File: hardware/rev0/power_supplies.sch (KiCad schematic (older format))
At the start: 40 parts, among them IC1 ECP5-BGA256, U2 MIC5504-1.8YM5, U3 MIC5219-3.3YM5, U4 TCR2EF11, U5 MIC5504-2.5YM5

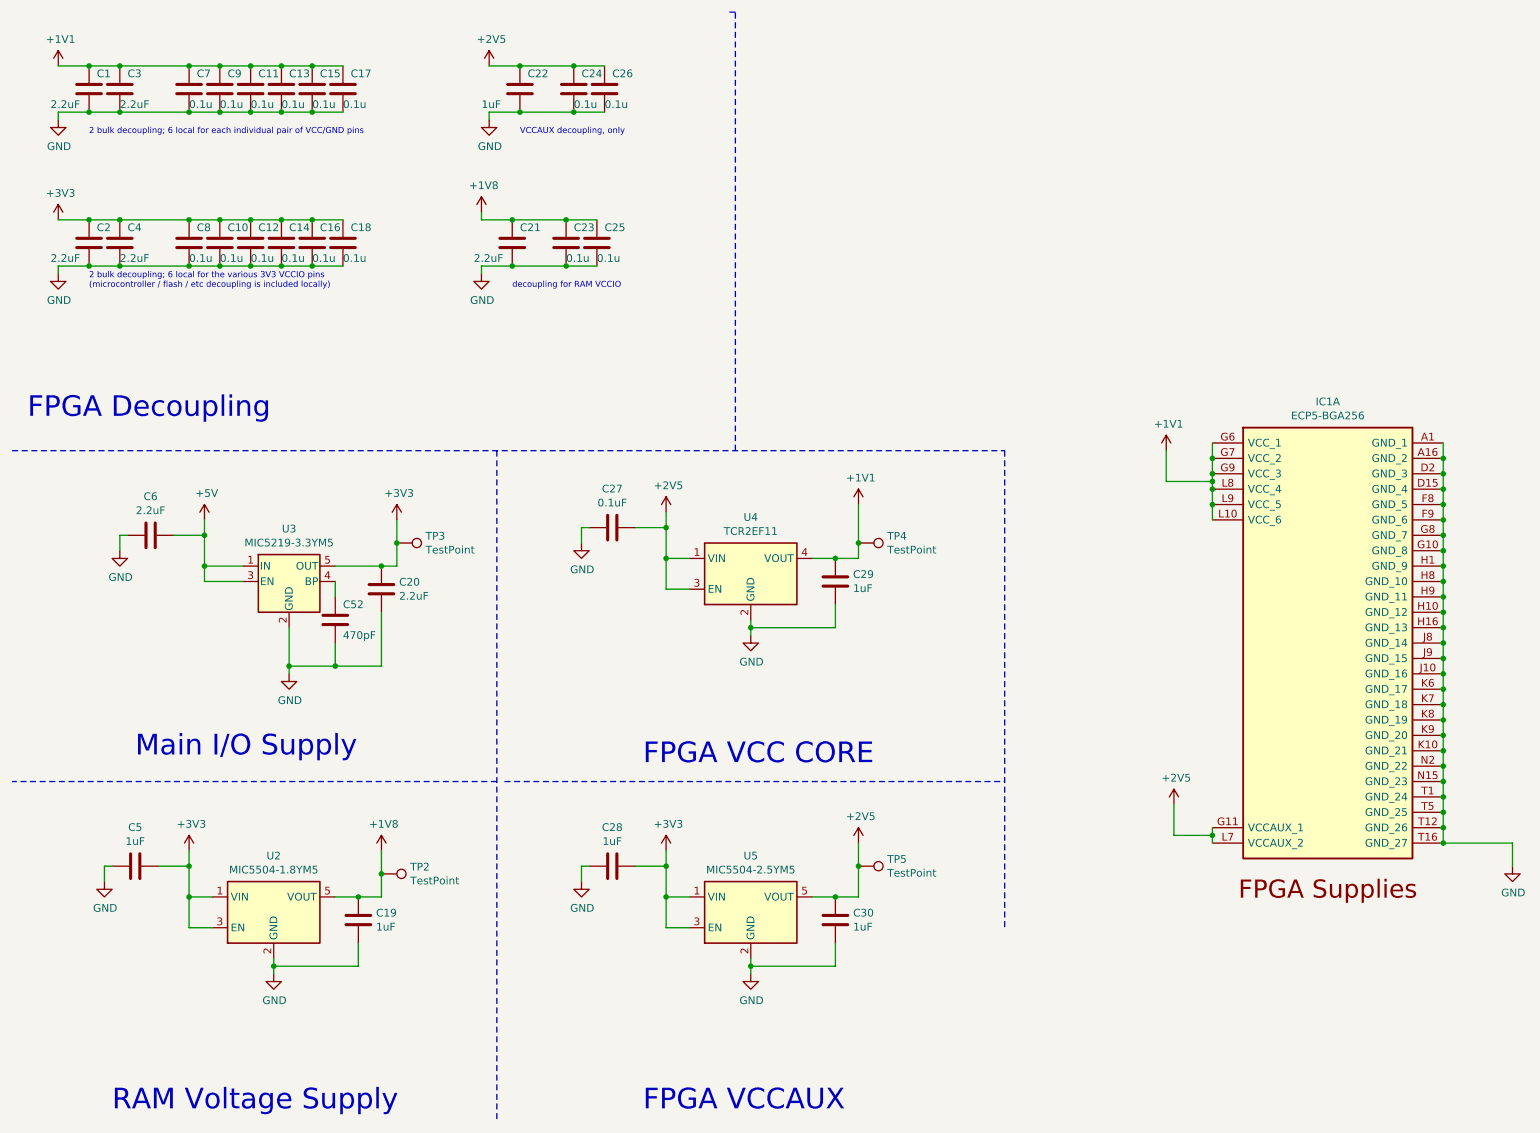
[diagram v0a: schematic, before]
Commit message: Switch to 3V3 for RAM, remove 1V8 rail
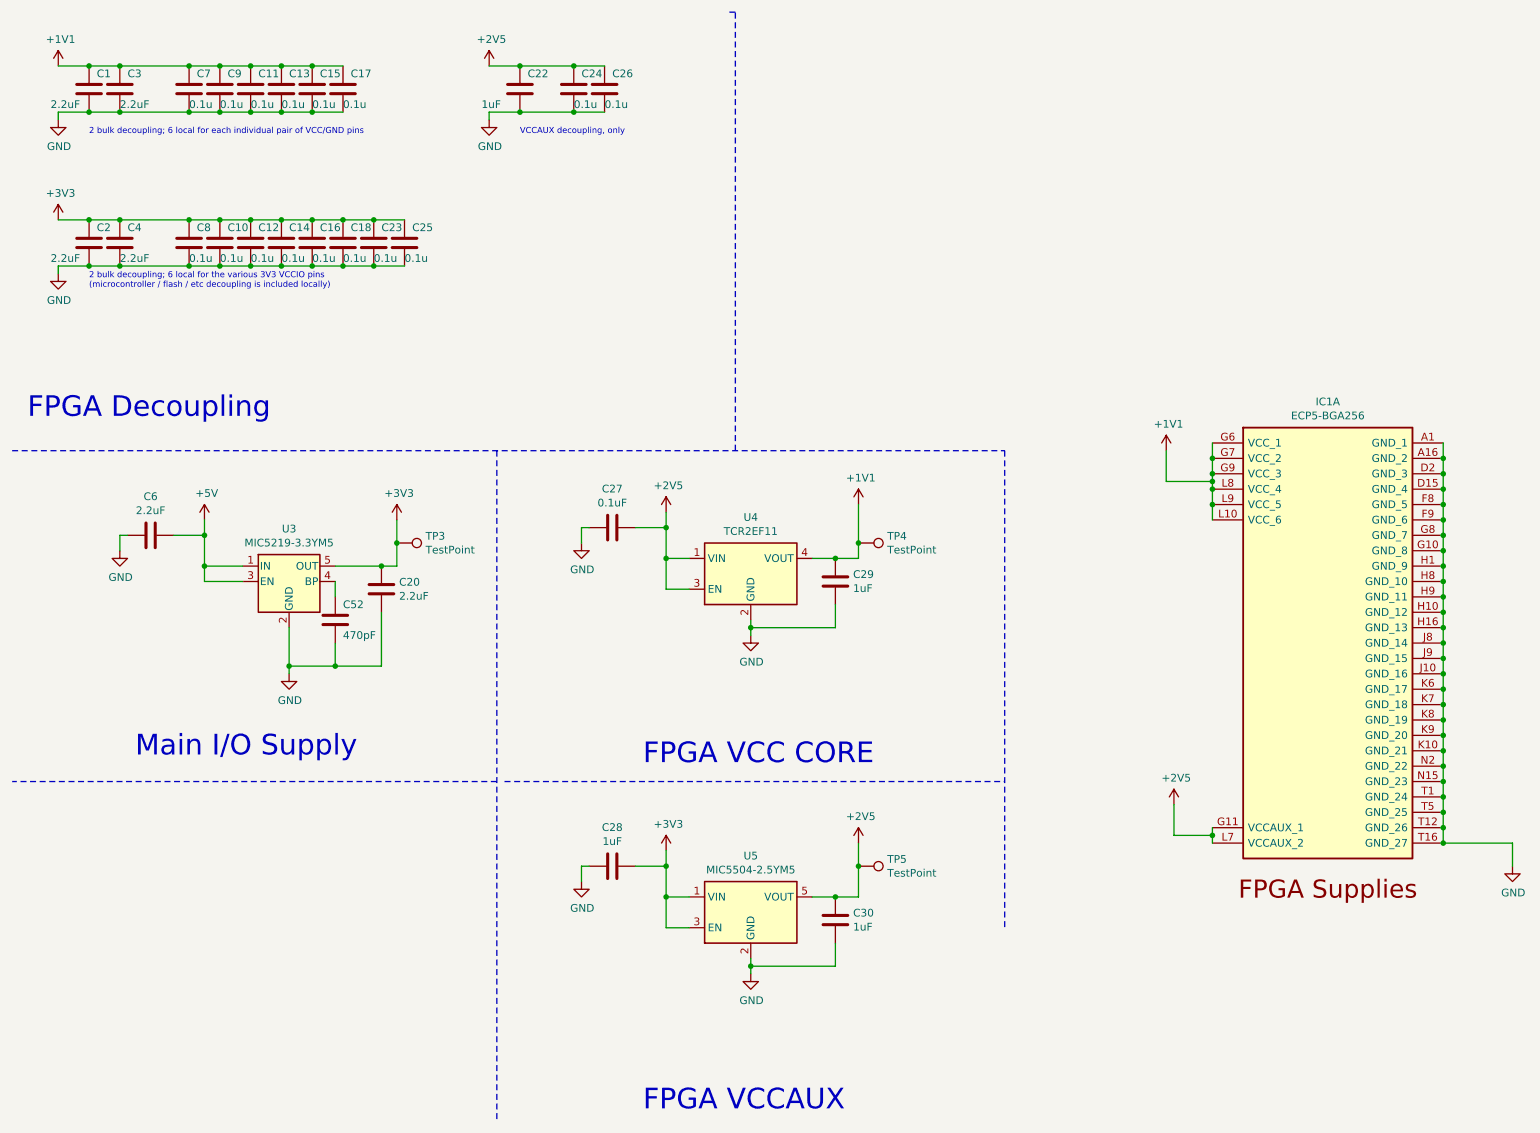
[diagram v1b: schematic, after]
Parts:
- removed C19, C5: 1uF, Capacitor_SMD:C_0603_1608Metric, symbol Device:C
- removed C21: 2.2uF, Capacitor_SMD:C_0603_1608Metric, symbol Device:C
- removed TP2: TestPoint, TestPoint:TestPoint_Pad_D1.0mm, symbol Connector:TestPoint
- removed U2: MIC5504-1.8YM5, Package_TO_SOT_SMD:SOT-23-5, symbol Regulator_Linear:MIC5504-1.8YM5
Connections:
- net +1V8 is gone; now on net +3V3: C23.1, C25.1
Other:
- note removed: "RAM Voltage Supply"
- note removed: "decoupling for RAM VCCIO"
- moved on the sheet: C23, C25
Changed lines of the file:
@@
 	1    0    0    -1
 $EndComp
-$Comp
-L Regulator_Linear:MIC5504-1.8YM5 U2
-U 1 1 5DAC1E40
-P 2250 6350
-F 0 "U2" H 2250 6717 50  0000 C CNN
-F 1 "MIC5504-1.8YM5" H 2250 6626 50  0000 C CNN
-F 2 "Package_TO_SOT_SMD:SOT-23-5" H 2250 5950 50  0001 C CNN
-F 3 "http://ww1.microchip.com/downloads/en/DeviceDoc/MIC550X.pdf" H 2000 6600 50  0001 C CNN
-	1    2250 6350
-	1    0    0    -1
-$EndComp
-Wire Wire Line
-	1850 6250 1700 6250
-$Comp
-L power:+3V3 #PWR018
-U 1 1 5DAC56AB
-P 1700 5950
-F 0 "#PWR018" H 1700 5800 50  0001 C CNN
-F 1 "+3V3" H 1715 6123 50  0000 C CNN
-F 2 "" H 1700 5950 50  0001 C CNN
-F 3 "" H 1700 5950 50  0001 C CNN
-	1    1700 5950
-	1    0    0    -1
-$EndComp
-Wire Wire Line
-	2250 6650 2250 6700
-$Comp
-L power:GND #PWR020
-U 1 1 5DAC8A3A
-P 2250 6750
-F 0 "#PWR020" H 2250 6500 50  0001 C CNN
-F 1 "GND" H 2255 6577 50  0000 C CNN
-F 2 "" H 2250 6750 50  0001 C CNN
-F 3 "" H 2250 6750 50  0001 C CNN
-	1    2250 6750
-	1    0    0    -1
-$EndComp
-Wire Wire Line
-	1700 5950 1700 6050
-$Comp
-L Device:C C5
-U 1 1 5DACA9F3
-P 1350 6050
-F 0 "C5" V 1098 6050 50  0000 C CNN
-F 1 "1uF" V 1189 6050 50  0000 C CNN
-F 2 "Capacitor_SMD:C_0603_1608Metric" H 1388 5900 50  0001 C CNN
-F 3 "~" H 1350 6050 50  0001 C CNN
-	1    1350 6050
-	0    1    1    0
-$EndComp
-Wire Wire Line
-	1150 6050 1200 6050
-Wire Wire Line
-	1150 6150 1150 6050
-$Comp
-L power:GND #PWR016
-U 1 1 5DACD5E8
-P 1150 6150
-F 0 "#PWR016" H 1150 5900 50  0001 C CNN
-F 1 "GND" H 1155 5977 50  0000 C CNN
-F 2 "" H 1150 6150 50  0001 C CNN
-F 3 "" H 1150 6150 50  0001 C CNN
-	1    1150 6150
-	1    0    0    -1
-$EndComp
-Connection ~ 1700 6050
-Wire Wire Line
-	1700 6050 1700 6250
-Wire Wire Line
-	2650 6250 2800 6250
-$Comp
-L power:+1V8 #PWR022
-U 1 1 5DAD001F
-P 2950 5950
-F 0 "#PWR022" H 2950 5800 50  0001 C CNN
-F 1 "+1V8" H 2965 6123 50  0000 C CNN
-F 2 "" H 2950 5950 50  0001 C CNN
-F 3 "" H 2950 5950 50  0001 C CNN
-	1    2950 5950
-	1    0    0    -1
-$EndComp
-Wire Wire Line
-	2950 5950 2950 6100
-$Comp
-L Device:C C19
-U 1 1 5DAD4777
-P 2800 6400
-F 0 "C19" H 2915 6446 50  0000 L CNN
-F 1 "1uF" H 2915 6355 50  0000 L CNN
-F 2 "Capacitor_SMD:C_0603_1608Metric" H 2838 6250 50  0001 C CNN
-F 3 "~" H 2800 6400 50  0001 C CNN
-	1    2800 6400
-	1    0    0    -1
-$EndComp
-Connection ~ 2800 6250
-Wire Wire Line
-	2800 6250 2950 6250
-Wire Wire Line
-	2800 6550 2800 6700
-Wire Wire Line
-	2800 6700 2250 6700
-Connection ~ 2250 6700
-Wire Wire Line
-	2250 6700 2250 6750
-Text Notes 1200 7650 0    134  ~ 0
-RAM Voltage Supply
 Wire Wire Line
 	4950 6250 4800 6250
@@
 $EndComp
 $Comp
-L Device:C C18
-U 1 1 5DBA82B3
-P 2700 2000
-F 0 "C18" H 2750 2100 50  0000 L CNN
-F 1 "0.1u" H 2700 1900 50  0000 L CNN
-F 2 "Capacitor_SMD:C_0402_1005Metric" H 2738 1850 50  0001 C CNN
-F 3 "~" H 2700 2000 50  0001 C CNN
-	1    2700 2000
-	1    0    0    -1
-$EndComp
-$Comp
 L Device:C C16
 U 1 1 5DBA82A9
@@
 Wire Wire Line
 	3850 850  4200 850
-Text Notes 3800 2300 0    39   ~ 0
-decoupling for RAM VCCIO
-$Comp
-L power:GND #PWR025
-U 1 1 5DC15F71
-P 3600 2200
-F 0 "#PWR025" H 3600 1950 50  0001 C CNN
-F 1 "GND" H 3605 2027 50  0000 C CNN
-F 2 "" H 3600 2200 50  0001 C CNN
-F 3 "" H 3600 2200 50  0001 C CNN
-	1    3600 2200
-	1    0    0    -1
-$EndComp
-Connection ~ 4150 2150
-Wire Wire Line
-	3800 2150 3600 2150
-Connection ~ 3800 2150
-Wire Wire Line
-	3600 2150 3600 2200
-Connection ~ 4150 1850
-Connection ~ 3800 1850
-Wire Wire Line
-	3600 1850 3800 1850
-$Comp
-L Device:C C21
-U 1 1 5DC15F82
-P 3800 2000
-F 0 "C21" H 3850 2100 50  0000 L CNN
-F 1 "2.2uF" H 3550 1900 50  0000 L CNN
-F 2 "Capacitor_SMD:C_0603_1608Metric" H 3838 1850 50  0001 C CNN
-F 3 "~" H 3800 2000 50  0001 C CNN
-	1    3800 2000
-	1    0    0    -1
-$EndComp
-$Comp
-L Device:C C23
-U 1 1 5DC15F8C
-P 4150 2000
-F 0 "C23" H 4200 2100 50  0000 L CNN
-F 1 "0.1u" H 4150 1900 50  0000 L CNN
-F 2 "Capacitor_SMD:C_0402_1005Metric" H 4188 1850 50  0001 C CNN
-F 3 "~" H 4150 2000 50  0001 C CNN
-	1    4150 2000
-	1    0    0    -1
-$EndComp
-Wire Wire Line
-	4350 2150 4150 2150
-Wire Wire Line
-	4150 1850 4350 1850
-$Comp
-L Device:C C25
-U 1 1 5DC15FA2
-P 4350 2000
-F 0 "C25" H 4400 2100 50  0000 L CNN
-F 1 "0.1u" H 4350 1900 50  0000 L CNN
-F 2 "Capacitor_SMD:C_0402_1005Metric" H 4388 1850 50  0001 C CNN
-F 3 "~" H 4350 2000 50  0001 C CNN
-	1    4350 2000
-	1    0    0    -1
-$EndComp
-Wire Wire Line
-	3800 2150 4150 2150
-Wire Wire Line
-	3800 1850 4150 1850
-$Comp
-L power:+1V8 #PWR024
-U 1 1 5DC20A72
-P 3600 1800
-F 0 "#PWR024" H 3600 1650 50  0001 C CNN
-F 1 "+1V8" H 3615 1973 50  0000 C CNN
-F 2 "" H 3600 1800 50  0001 C CNN
-F 3 "" H 3600 1800 50  0001 C CNN
-	1    3600 1800
-	1    0    0    -1
-$EndComp
-Wire Wire Line
-	3600 1800 3600 1850
 Wire Notes Line
 	5250 3350 5250 500
@@
 Wire Wire Line
 	4800 4250 4950 4250
-Wire Wire Line
-	1500 6050 1700 6050
-Wire Wire Line
-	1850 6450 1700 6450
-Wire Wire Line
-	1700 6450 1700 6250
-Connection ~ 1700 6250
 Wire Wire Line
 	4800 6250 4800 6450
@@
 	6050 6050 6050 6250
 $Comp
-L Connector:TestPoint TP2
-U 1 1 5E2192C9
-P 2950 6100
-F 0 "TP2" V 2905 6287 50  0000 L CNN
-F 1 "TestPoint" V 2995 6287 50  0000 L CNN
-F 2 "TestPoint:TestPoint_Pad_D1.0mm" H 3150 6100 50  0001 C CNN
-F 3 "~" H 3150 6100 50  0001 C CNN
-	1    2950 6100
-	0    1    1    0
-$EndComp
-Connection ~ 2950 6100
-Wire Wire Line
-	2950 6100 2950 6250
+L Device:C C25
+U 1 1 5DC15FA2
+P 3100 2000
+F 0 "C25" H 3150 2100 50  0000 L CNN
+F 1 "0.1u" H 3100 1900 50  0000 L CNN
+F 2 "Capacitor_SMD:C_0402_1005Metric" H 3138 1850 50  0001 C CNN
+F 3 "~" H 3100 2000 50  0001 C CNN
+	1    3100 2000
+	1    0    0    -1
+$EndComp
+$Comp
+L Device:C C23
+U 1 1 5DC15F8C
+P 2900 2000
+F 0 "C23" H 2950 2100 50  0000 L CNN
+F 1 "0.1u" H 2900 1900 50  0000 L CNN
+F 2 "Capacitor_SMD:C_0402_1005Metric" H 2938 1850 50  0001 C CNN
+F 3 "~" H 2900 2000 50  0001 C CNN
+	1    2900 2000
+	1    0    0    -1
+$EndComp
+Wire Wire Line
+	2900 1850 3100 1850
+Wire Wire Line
+	3100 2150 2900 2150
+$Comp
+L Device:C C18
+U 1 1 5DBA82B3
+P 2700 2000
+F 0 "C18" H 2750 2100 50  0000 L CNN
+F 1 "0.1u" H 2700 1900 50  0000 L CNN
+F 2 "Capacitor_SMD:C_0402_1005Metric" H 2738 1850 50  0001 C CNN
+F 3 "~" H 2700 2000 50  0001 C CNN
+	1    2700 2000
+	1    0    0    -1
+$EndComp
+Wire Wire Line
+	2700 1850 2900 1850
+Connection ~ 2700 1850
+Connection ~ 2900 1850
+Wire Wire Line
+	2700 2150 2900 2150
+Connection ~ 2700 2150
+Connection ~ 2900 2150
 $EndSCHEMATC

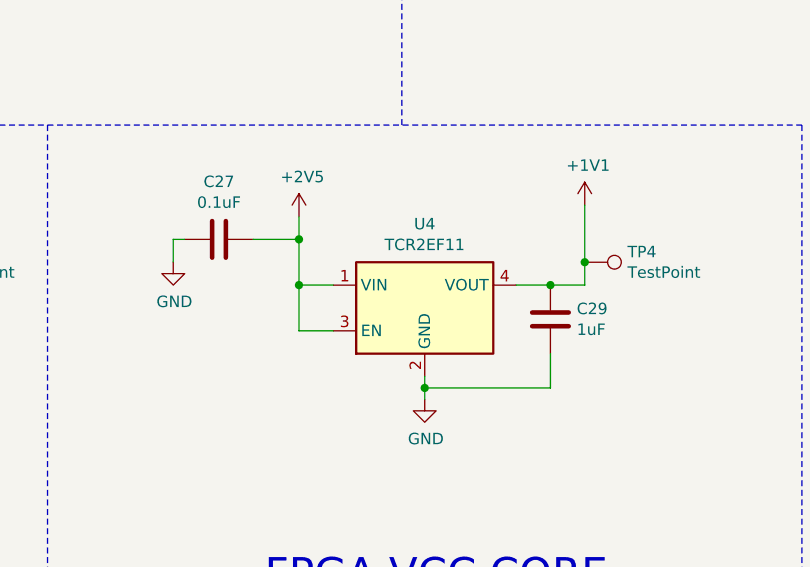
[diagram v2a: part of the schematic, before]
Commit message: Fix TCR2EE footprint
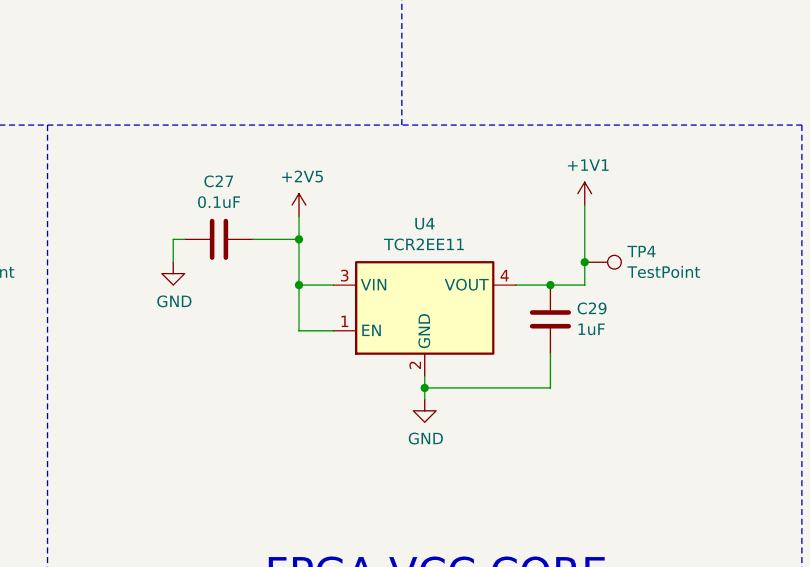
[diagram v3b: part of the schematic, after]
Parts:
- removed U4: TCR2EF11, Package_TO_SOT_SMD:SOT-553, symbol support_hardware:TCR2EF11
- added U4: TCR2EE11, Package_TO_SOT_SMD:SOT-553, symbol support_hardware:TCR2EE11
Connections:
- net +1V1: now also U4.4 (VOUT)
- net +2V5: now also U4.1 (EN), U4.3 (VIN)
- net GND: now also U4.2 (GND)
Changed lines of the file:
@@
 	550  3350 7000 3350
-$Comp
-L support_hardware:TCR2EF11 U4
-U 1 1 5DB6F5E4
-P 5350 4150
-F 0 "U4" H 5350 4517 50  0000 C CNN
-F 1 "TCR2EF11" H 5350 4426 50  0000 C CNN
-F 2 "Package_TO_SOT_SMD:SOT-553" H 5350 3750 50  0001 C CNN
-F 3 "https://toshiba.semicon-storage.com/info/docget.jsp?did=13794&prodName=TCR2EF45" H 5100 4400 50  0001 C CNN
-	1    5350 4150
-	1    0    0    -1
-$EndComp
 $Comp
 L power:+2V5 #PWR030
@@
 Wire Wire Line
 	5900 4050 6050 4050
+$Comp
+L support_hardware:TCR2EE11 U4
+U 1 1 5ED4FF7D
+P 5350 4150
+F 0 "U4" H 5350 4517 50  0000 C CNN
+F 1 "TCR2EE11" H 5350 4426 50  0000 C CNN
+F 2 "Package_TO_SOT_SMD:SOT-553" H 5350 3750 50  0001 C CNN
+F 3 "https://toshiba.semicon-storage.com/info/docget.jsp?did=13794&prodName=TCR2EF45" H 5100 4400 50  0001 C CNN
+	1    5350 4150
+	1    0    0    -1
+$EndComp
 $EndSCHEMATC
